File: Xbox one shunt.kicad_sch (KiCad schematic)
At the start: 13 parts, among them U1 INA181A1-Q1, U2 TLV3201AIDCKR

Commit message: added a U.FL SMT conector for an osciloscope
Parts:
- added J1, J2: U.FL-R-SMT-1_10_, U.FL-R-SMT-1_10:HRS_U.FL-R-SMT-1_10_, symbol U.FL_R_SMT_1:U.FL-R-SMT-1_10_
- renumbered TP4 to 3V3, TP1 to CMP1, TP5 to GND1
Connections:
- net AMP_OUT: now also J1.2
- net CMP_OUT: now also J2.2
- net GND: now also J1.1, J1.3, J2.1, J2.3

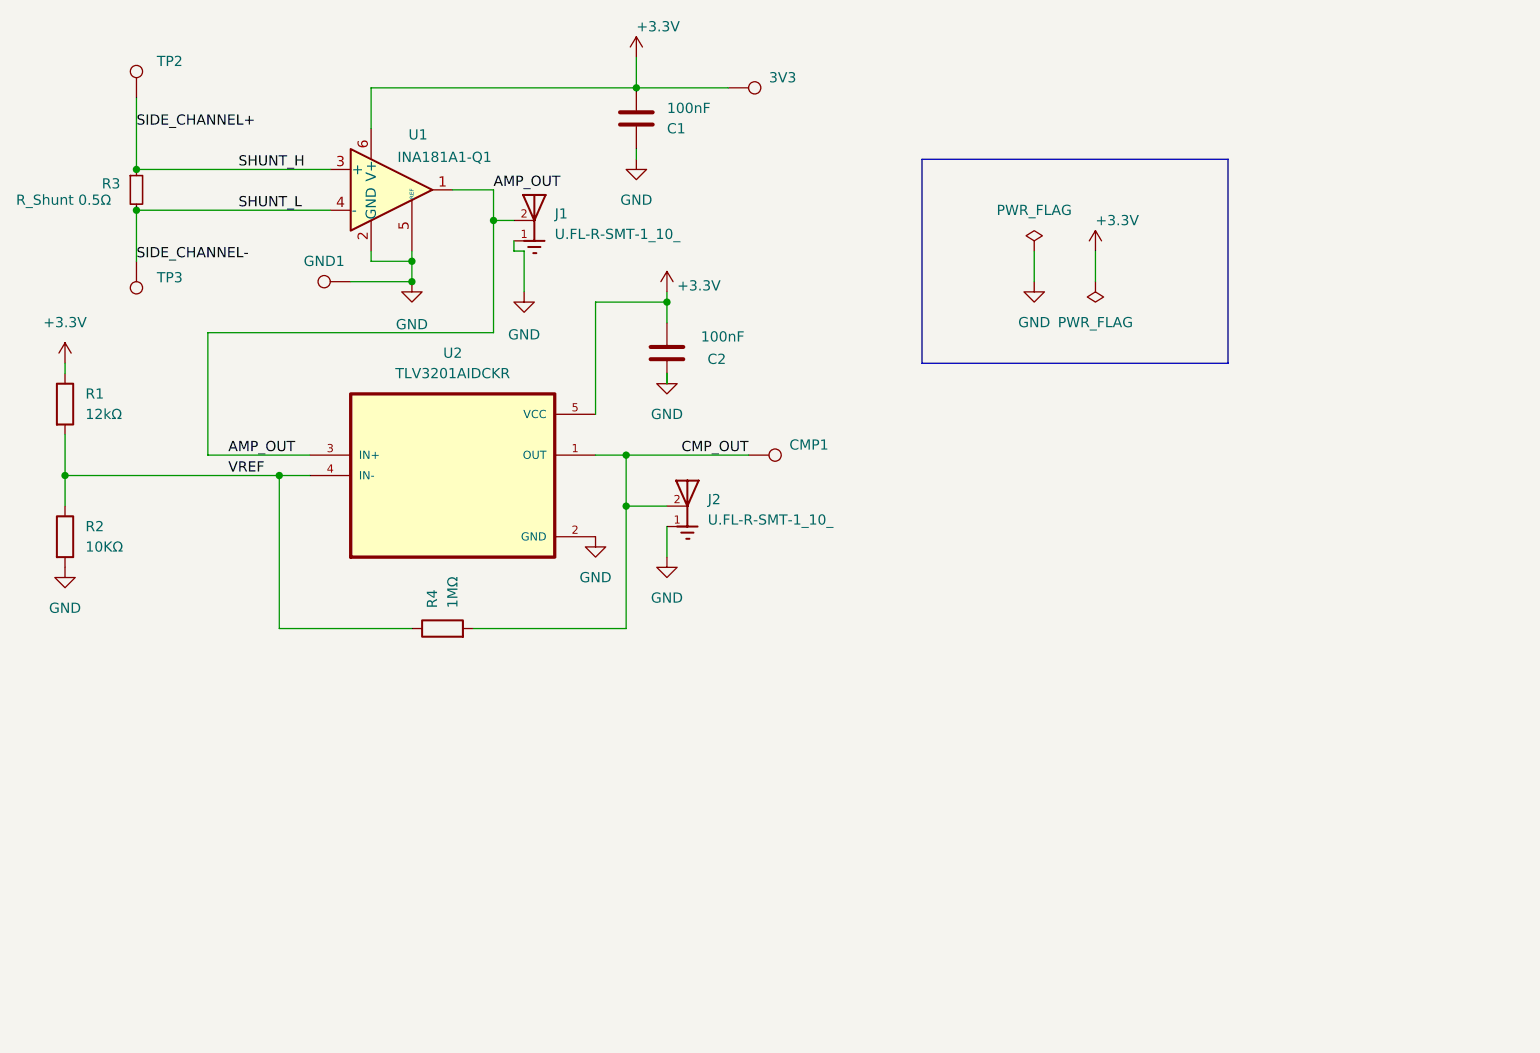
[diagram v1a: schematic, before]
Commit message: pcb and sch fixes
Replaced TLV3201AIDCKR (SC70-5) which was using an SOT-23-5 footprint with a TLV3201AIDBVR (same specs and correct footprint)
Updated schematic and PCB for above change
Added Libraries directory and applied to project
Edited symbols
Fixed silks
Added 3D models
Some general cleaning in schematic and PCB
Clean DRC
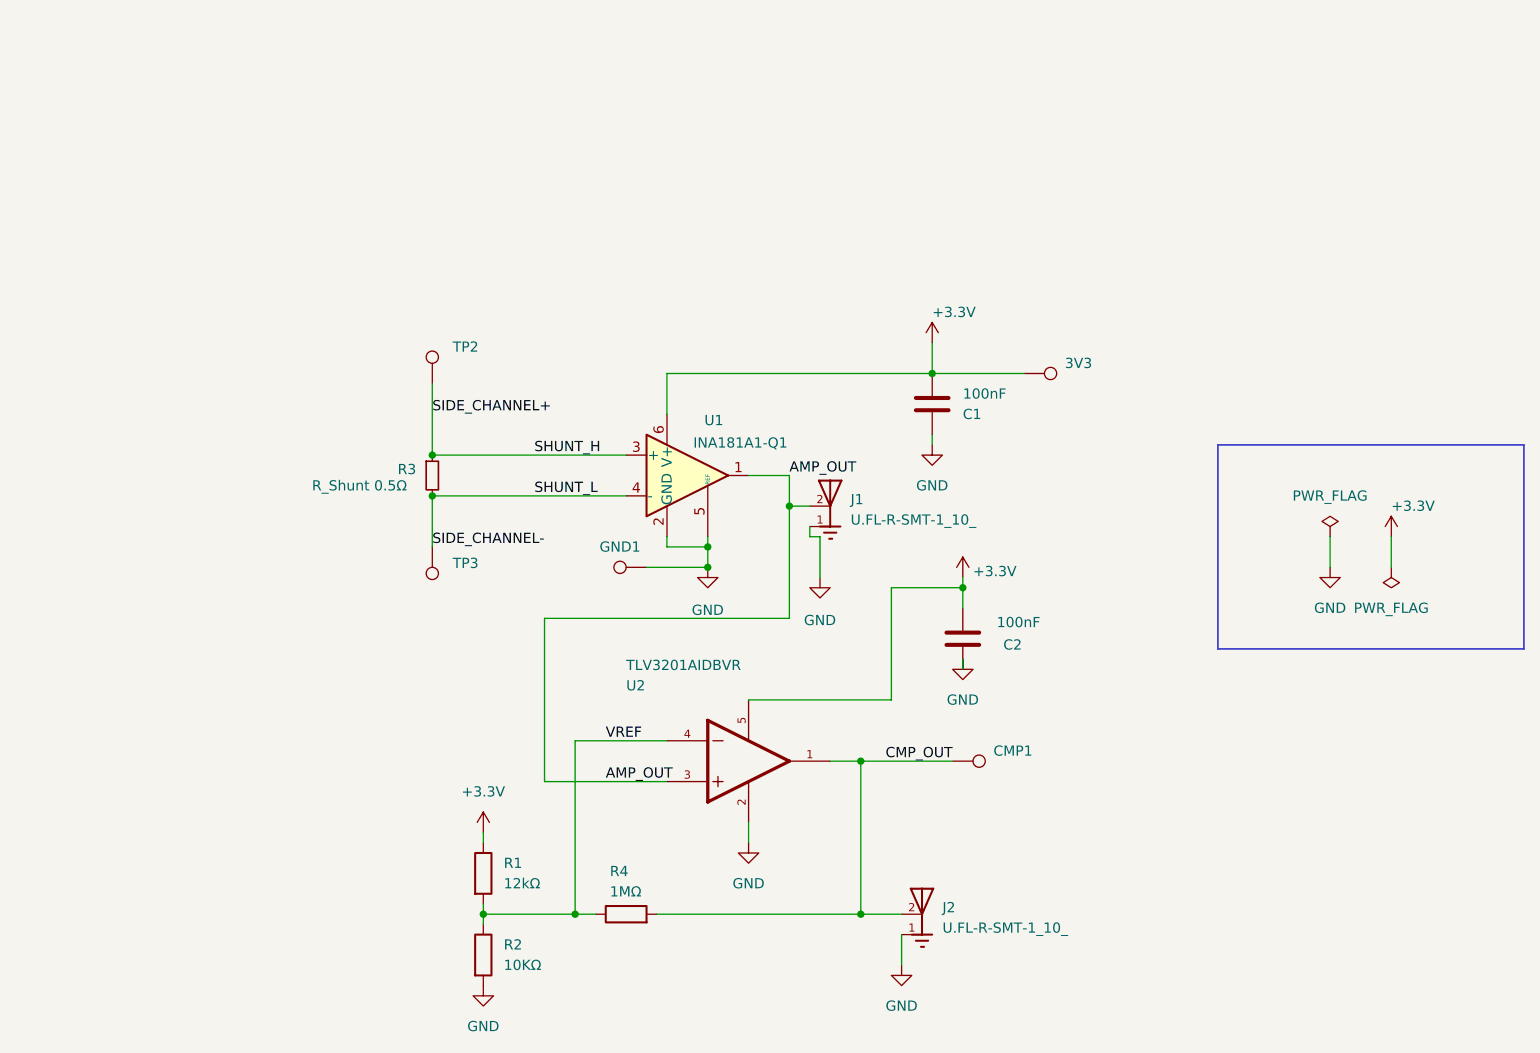
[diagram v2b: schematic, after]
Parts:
- removed U2: TLV3201AIDCKR, Package_TO_SOT_SMD:SOT-23-5, symbol TLV3201AIDCKR:TLV3201AIDCKR
- added U2: TLV3201AIDBVR, TLV3201AIDBVR:TLV3201AIDBVR, symbol TLV3201AIDBVR:TLV3201AIDBVR
- J1, J2: footprint U.FL-R-SMT-1_10:HRS_U.FL-R-SMT-1_10_ -> U.FL-R-SMT-1_10_:HRS_U.FL-R-SMT-1_10_; symbol U.FL_R_SMT_1:U.FL-R-SMT-1_10_ -> HRS_U.FL-R-SMT-1_10_:U.FL-R-SMT-1_10_
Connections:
- net +3.3V: now also U2.5
- net AMP_OUT: now also U2.3
- net CMP_OUT: now also U2.1
- net GND: now also U2.2
- net VREF: now also U2.4
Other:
- moved on the sheet: 3V3, C1, C2, CMP1, GND1, J1, J2, R1, R2, R3, R4, TP2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
